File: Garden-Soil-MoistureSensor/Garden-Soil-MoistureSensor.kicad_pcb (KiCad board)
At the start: 2 copper layers, 6 parts, among them J1 Conn_01x15, J2 Conn_01x15, J3 Screw_Terminal_01x02, J4 Screw_Terminal_01x02, Q1 BD140

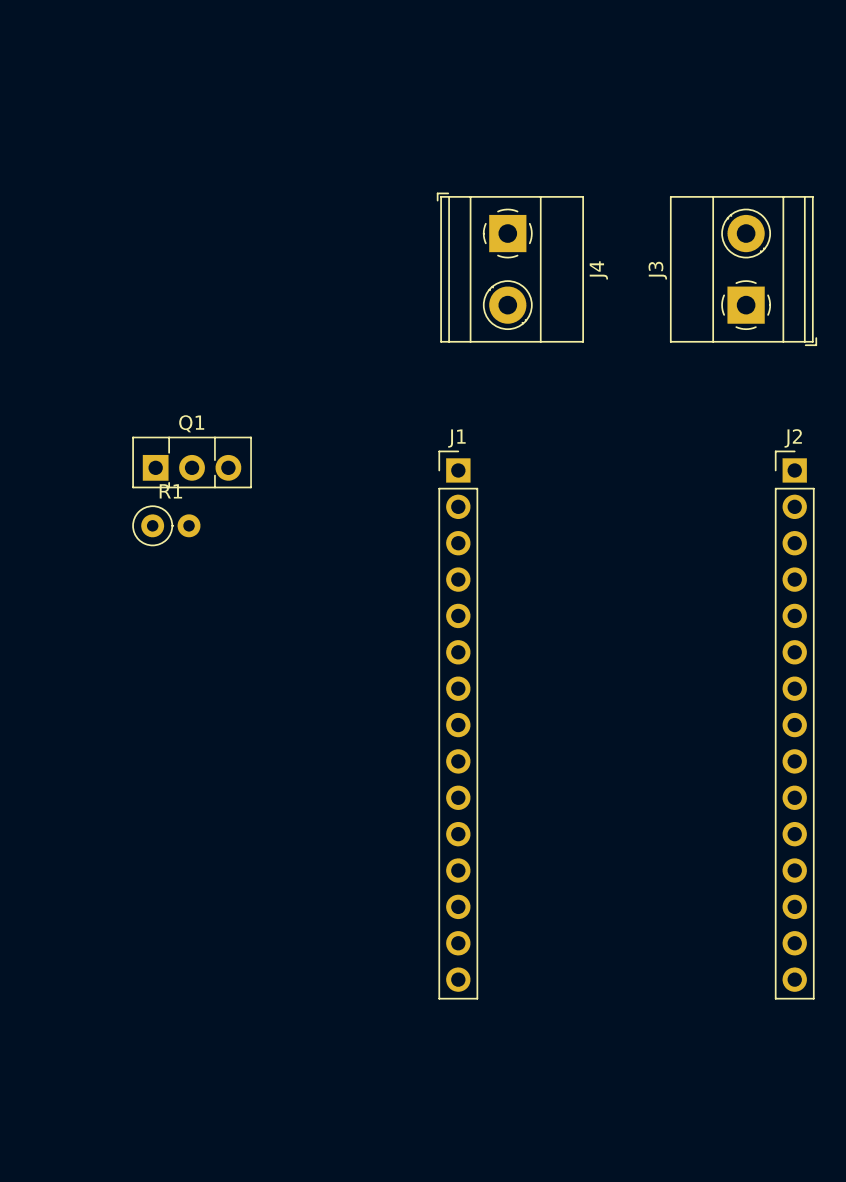
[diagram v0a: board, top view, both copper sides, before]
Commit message: adding a PCB mount 18650 battery holder.
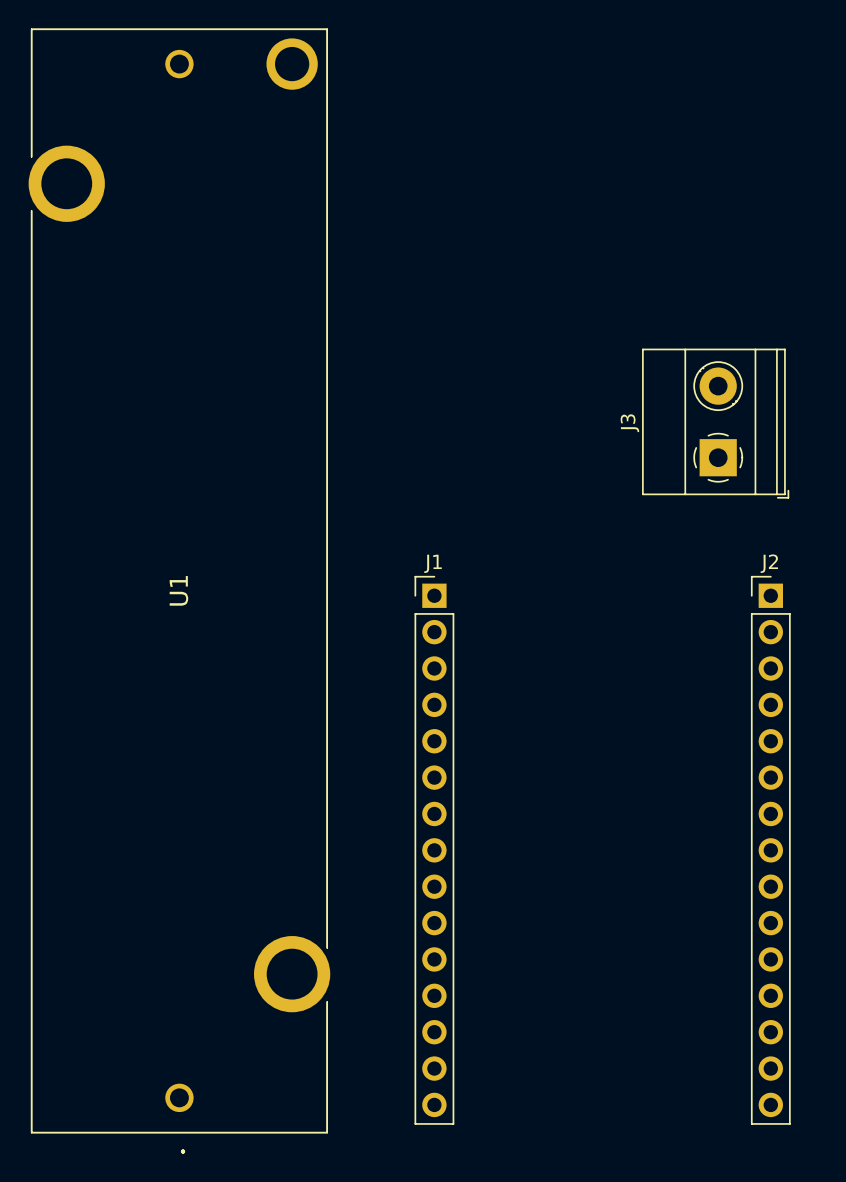
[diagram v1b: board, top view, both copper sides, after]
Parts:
- removed J4: Screw_Terminal_01x02, TerminalBlock_Phoenix:TerminalBlock_Phoenix_MKDS-1,5-2_1x02_P5.00mm_Horizontal
- removed Q1: BD140, Package_TO_SOT_THT:TO-126-3_Vertical
- removed R1: 4.7K, Resistor_THT:R_Axial_DIN0207_L6.3mm_D2.5mm_P2.54mm_Vertical
- added U1: 1043, SamacSys_Parts:1043, F.Cu at (132.9, 130.2)
- moved J3 10.8 mm to (170.6, 85.5)
- moved J1 8.91 mm to (150.7, 95.1)
- moved J2 8.91 mm to (174.2, 95.1)

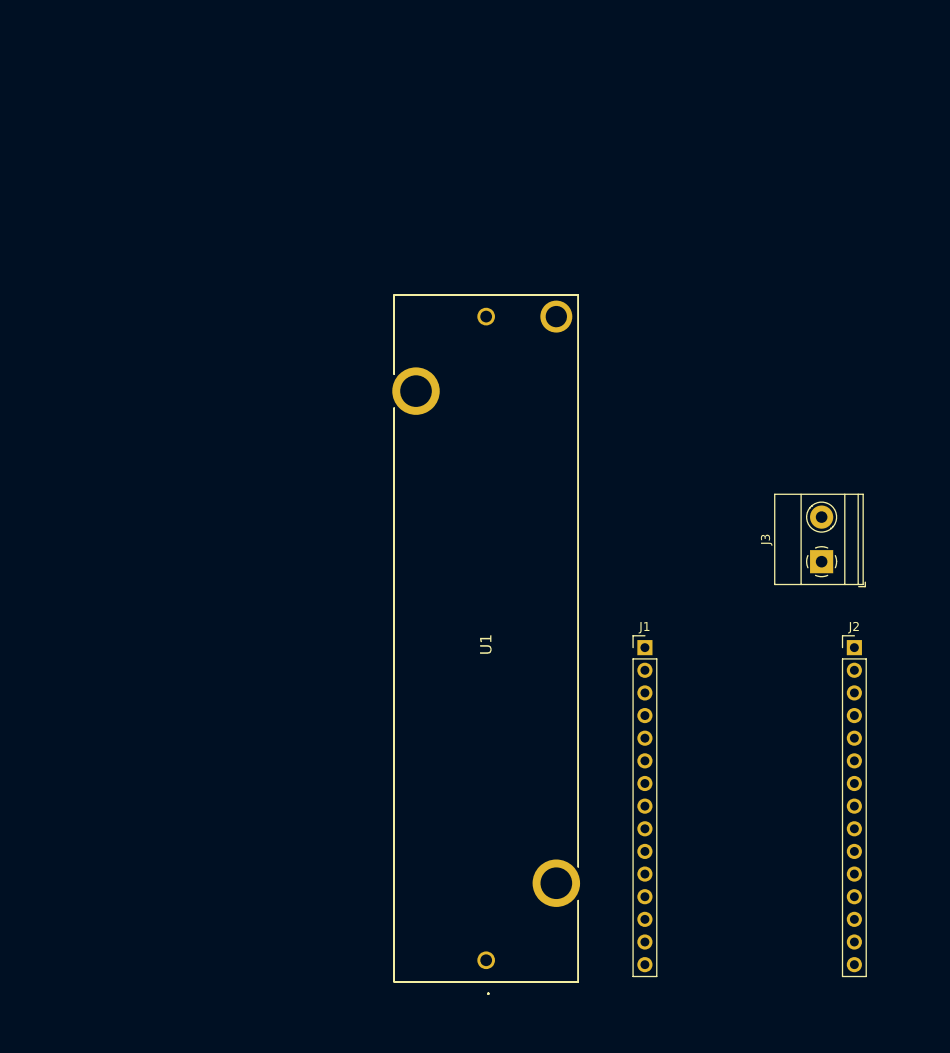
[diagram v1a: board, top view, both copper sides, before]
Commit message: doing some routing and footprint assignments.
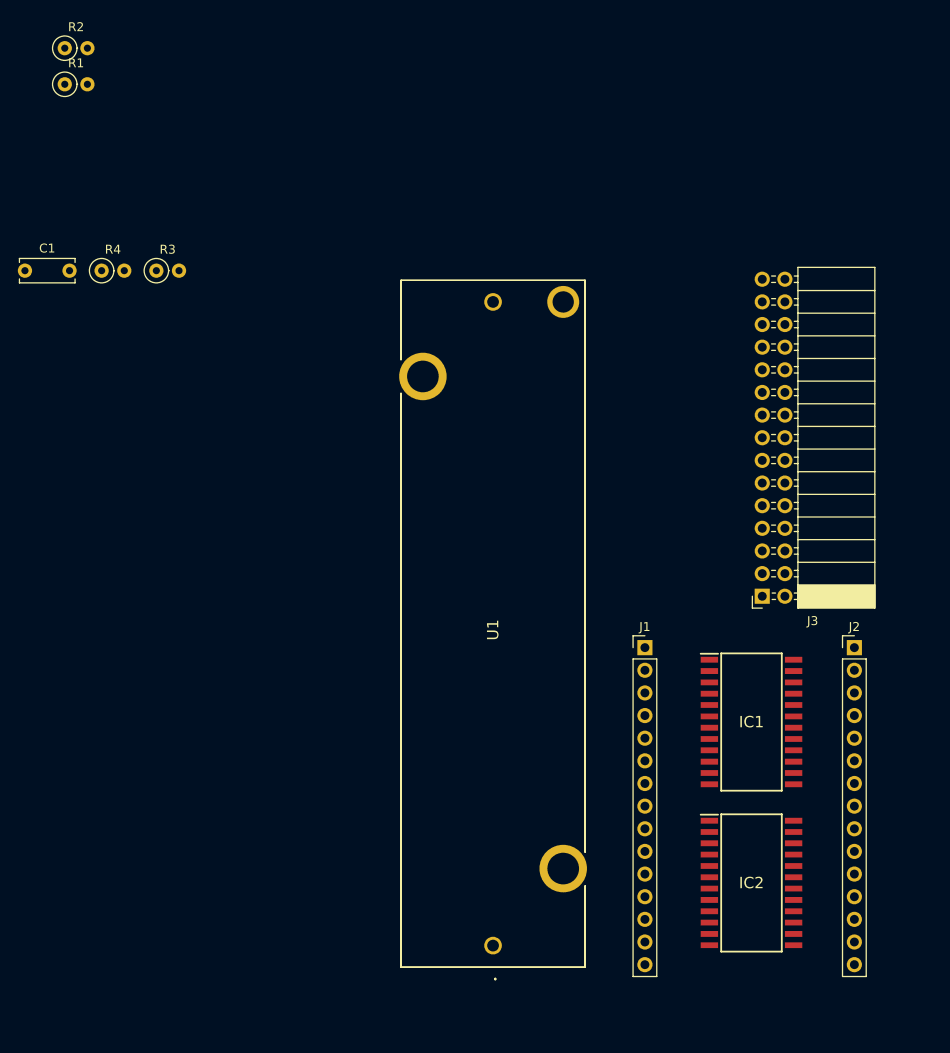
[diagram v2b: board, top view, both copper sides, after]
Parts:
- added C1: 0.1uF, Capacitor_THT:C_Disc_D6.0mm_W2.5mm_P5.00mm, F.Cu at (81.2, 52.8)
- added IC1: CD74HC4067M96, SamacSys_Parts:SOIC127P1030X265-24N, F.Cu at (162.7, 103.5)
- added IC2: CD74HC4067M96, SamacSys_Parts:SOIC127P1030X265-24N, F.Cu at (162.7, 121.5)
- added R1: 1M, Resistor_THT:R_Axial_DIN0207_L6.3mm_D2.5mm_P2.54mm_Vertical, F.Cu at (85.7, 31.9)
- added R2: 10K, Resistor_THT:R_Axial_DIN0207_L6.3mm_D2.5mm_P2.54mm_Vertical, F.Cu at (85.7, 27.9)
- added R3: 10k, Resistor_THT:R_Axial_DIN0207_L6.3mm_D2.5mm_P2.54mm_Vertical, F.Cu at (95.9, 52.8)
- added R4: 10k, Resistor_THT:R_Axial_DIN0207_L6.3mm_D2.5mm_P2.54mm_Vertical, F.Cu at (89.8, 52.8)
- J3: value Screw_Terminal_01x02 -> Conn_02x15_Odd_Even; footprint TerminalBlock_Phoenix:TerminalBlock_Phoenix_MKDS-1,5-2_1x02_P5.00mm_Horizontal -> Connector_PinSocket_2.54mm:PinSocket_2x15_P2.54mm_Horizontal
- moved J3 7.71 mm to (163.9, 89.3), turned to 180 degrees
- moved U1 1.82 mm to (133.7, 128.5)
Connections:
- J3 pad 1: D3 -> 1B
- J3 pad 2: A0 -> 1A
- U1 pad MH1: unconnected-(U1-PadMH1) -> VIN
- U1 pad MH2: unconnected-(U1-PadMH2) -> GND
- U1 pad MH3: unconnected-(U1-PadMH3) -> GND

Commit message: basic placement pre route
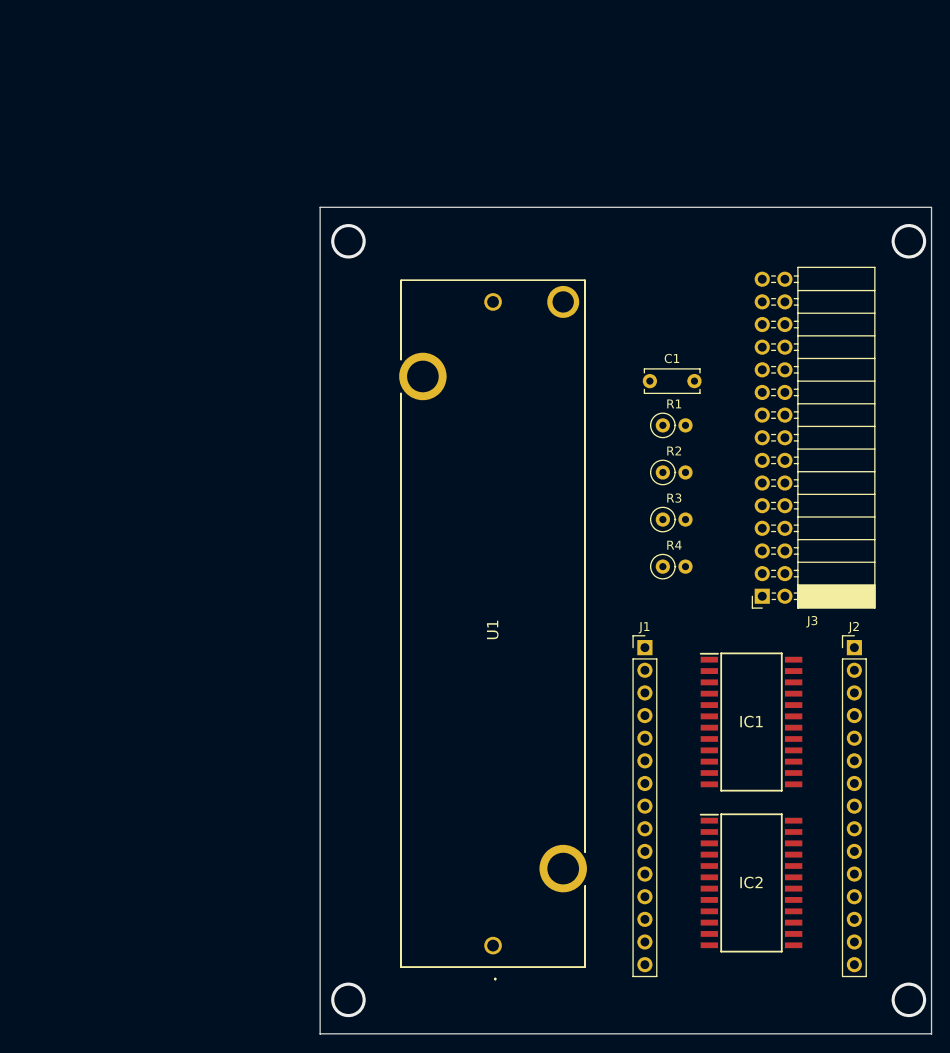
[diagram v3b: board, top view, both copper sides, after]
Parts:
- moved R2 82.3 mm to (152.7, 75.5)
- moved R1 77.2 mm to (152.7, 70.2)
- moved C1 71.2 mm to (151.3, 65.2)
- moved R4 71.2 mm to (152.7, 86.0)
- moved R3 63.3 mm to (152.7, 80.7)
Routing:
- net GND: vias 0 -> 4
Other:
- board outline added: 68.6 x 92.8 mm
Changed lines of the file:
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@@
   (net 33 "2B")
   (net 34 "1B")
-  (net 35 "Net-(IC2-Pad9)")
+  (net 35 "Net-(IC1-Pad9)")
   (net 36 "15B")
   (net 37 "14B")
@@
   (net 58 "8A")
   (footprint "Resistor_THT:R_Axial_DIN0207_L6.3mm_D2.5mm_P2.54mm_Vertical" (layer "F.Cu")
-    (at 89.78908 52.826146)
+    (at 152.742764 86.023614)
     (descr "Resistor, Axial_DIN0207 series, Axial, Vertical, pin pitch=2.54mm, 0.25W = 1/4W, length*diameter=6.3*2.5mm^2, http://cdn-reichelt.de/documents/datenblatt/B400/1_4W%23YAG.pdf")
     (tags "Resistor Axial_DIN0207 series Axial Vertical pin pitch 2.54mm 0.25W = 1/4W length 6.3mm diameter 2.5mm")
@@
   )
   (footprint "Resistor_THT:R_Axial_DIN0207_L6.3mm_D2.5mm_P2.54mm_Vertical" (layer "F.Cu")
-    (at 85.654047 27.869494)
+    (at 152.742764 75.462029)
     (descr "Resistor, Axial_DIN0207 series, Axial, Vertical, pin pitch=2.54mm, 0.25W = 1/4W, length*diameter=6.3*2.5mm^2, http://cdn-reichelt.de/documents/datenblatt/B400/1_4W%23YAG.pdf")
     (tags "Resistor Axial_DIN0207 series Axial Vertical pin pitch 2.54mm 0.25W = 1/4W length 6.3mm diameter 2.5mm")
@@
   )
   (footprint "Resistor_THT:R_Axial_DIN0207_L6.3mm_D2.5mm_P2.54mm_Vertical" (layer "F.Cu")
-    (at 85.654047 31.919494)
+    (at 152.742764 70.181237)
     (descr "Resistor, Axial_DIN0207 series, Axial, Vertical, pin pitch=2.54mm, 0.25W = 1/4W, length*diameter=6.3*2.5mm^2, http://cdn-reichelt.de/documents/datenblatt/B400/1_4W%23YAG.pdf")
     (tags "Resistor Axial_DIN0207 series Axial Vertical pin pitch 2.54mm 0.25W = 1/4W length 6.3mm diameter 2.5mm")
@@
   )
   (footprint "Resistor_THT:R_Axial_DIN0207_L6.3mm_D2.5mm_P2.54mm_Vertical" (layer "F.Cu")
-    (at 95.92908 52.826146)
+    (at 152.742764 80.742821)
     (descr "Resistor, Axial_DIN0207 series, Axial, Vertical, pin pitch=2.54mm, 0.25W = 1/4W, length*diameter=6.3*2.5mm^2, http://cdn-reichelt.de/documents/datenblatt/B400/1_4W%23YAG.pdf")
     (tags "Resistor Axial_DIN0207 series Axial Vertical pin pitch 2.54mm 0.25W = 1/4W length 6.3mm diameter 2.5mm")
@@
       (net 34 "1B") (pinfunction "I1") (pintype "passive"))
     (pad "9" smd rect locked (at -4.725 3.175 90) (size 0.65 1.95) (layers "F.Cu" "F.Paste" "F.Mask")
-      (net 35 "Net-(IC2-Pad9)") (pinfunction "I0") (pintype "passive"))
+      (net 35 "Net-(IC1-Pad9)") (pinfunction "I0") (pintype "passive"))
     (pad "10" smd rect locked (at -4.725 4.445 90) (size 0.65 1.95) (layers "F.Cu" "F.Paste" "F.Mask")
       (net 15 "D1") (pinfunction "S0") (pintype "passive"))
@@
   )
   (footprint "Capacitor_THT:C_Disc_D6.0mm_W2.5mm_P5.00mm" (layer "F.Cu")
-    (at 81.18908 52.826146)
+    (at 151.287764 65.215488)
     (descr "C, Disc series, Radial, pin pitch=5.00mm, , diameter*width=6*2.5mm^2, Capacitor, http://cdn-reichelt.de/documents/datenblatt/B300/DS_KERKO_TC.pdf")
     (tags "C Disc series Radial pin pitch 5.00mm  diameter 6mm width 2.5mm Capacitor")
@@
       (net 50 "1A") (pinfunction "I1") (pintype "passive"))
     (pad "9" smd rect locked (at -4.725 3.175 90) (size 0.65 1.95) (layers "F.Cu" "F.Paste" "F.Mask")
-      (net 35 "Net-(IC2-Pad9)") (pinfunction "I0") (pintype "passive"))
+      (net 35 "Net-(IC1-Pad9)") (pinfunction "I0") (pintype "passive"))
     (pad "10" smd rect locked (at -4.725 4.445 90) (size 0.65 1.95) (layers "F.Cu" "F.Paste" "F.Mask")
       (net 15 "D1") (pinfunction "S0") (pintype "passive"))
@@
     )
   )
+  (gr_line (start 114.3 45.72) (end 114.3 138.475913) (layer "Edge.Cuts") (width 0.1))
+  (gr_line (start 182.88 45.72) (end 114.3 45.72) (layer "Edge.Cuts") (width 0.1))
+  (gr_line (start 114.3 138.43) (end 182.88 138.43) (layer "Edge.Cuts") (width 0.1))
+  (gr_line (start 182.88 138.48139) (end 182.88 45.754492) (layer "Edge.Cuts") (width 0.1))
+  (via (at 117.475 49.53) (size 3.8736) (drill 3.175) (layers "F.Cu" "B.Cu") (free) (net 10))
+  (via (at 117.475 134.62) (size 3.8736) (drill 3.175) (layers "F.Cu" "B.Cu") (free) (net 10))
+  (via (at 180.34 49.53) (size 3.8736) (drill 3.175) (layers "F.Cu" "B.Cu") (free) (net 10))
+  (via (at 180.34 134.62) (size 3.8736) (drill 3.175) (layers "F.Cu" "B.Cu") (free) (net 10))
   (group "" (id 31916c38-883f-4186-ab10-8bd6d91959f5)
     (members

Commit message: drc fixes pre route
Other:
- board size 68.6 x 92.8 mm -> 68.6 x 92.7 mm
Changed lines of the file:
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@@
     )
   )
-  (gr_line (start 114.3 45.72) (end 114.3 138.475913) (layer "Edge.Cuts") (width 0.1))
+  (gr_line (start 114.3 45.72) (end 114.3 138.43) (layer "Edge.Cuts") (width 0.1))
   (gr_line (start 182.88 45.72) (end 114.3 45.72) (layer "Edge.Cuts") (width 0.1))
   (gr_line (start 114.3 138.43) (end 182.88 138.43) (layer "Edge.Cuts") (width 0.1))
-  (gr_line (start 182.88 138.48139) (end 182.88 45.754492) (layer "Edge.Cuts") (width 0.1))
+  (gr_line (start 182.88 138.43) (end 182.88 45.72) (layer "Edge.Cuts") (width 0.1))
   (via (at 117.475 49.53) (size 3.8736) (drill 3.175) (layers "F.Cu" "B.Cu") (free) (net 10))
   (via (at 117.475 134.62) (size 3.8736) (drill 3.175) (layers "F.Cu" "B.Cu") (free) (net 10))

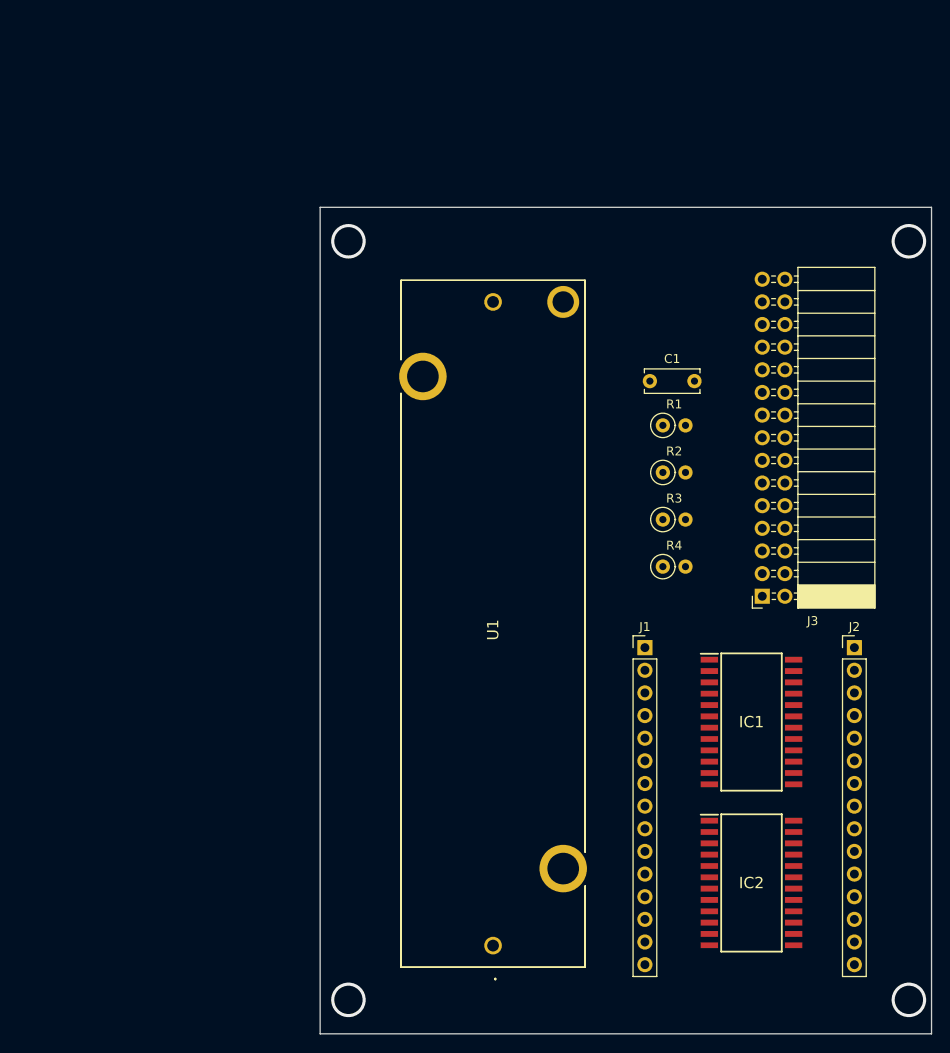
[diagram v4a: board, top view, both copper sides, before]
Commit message: post route needs to have silkscreen labels applied.
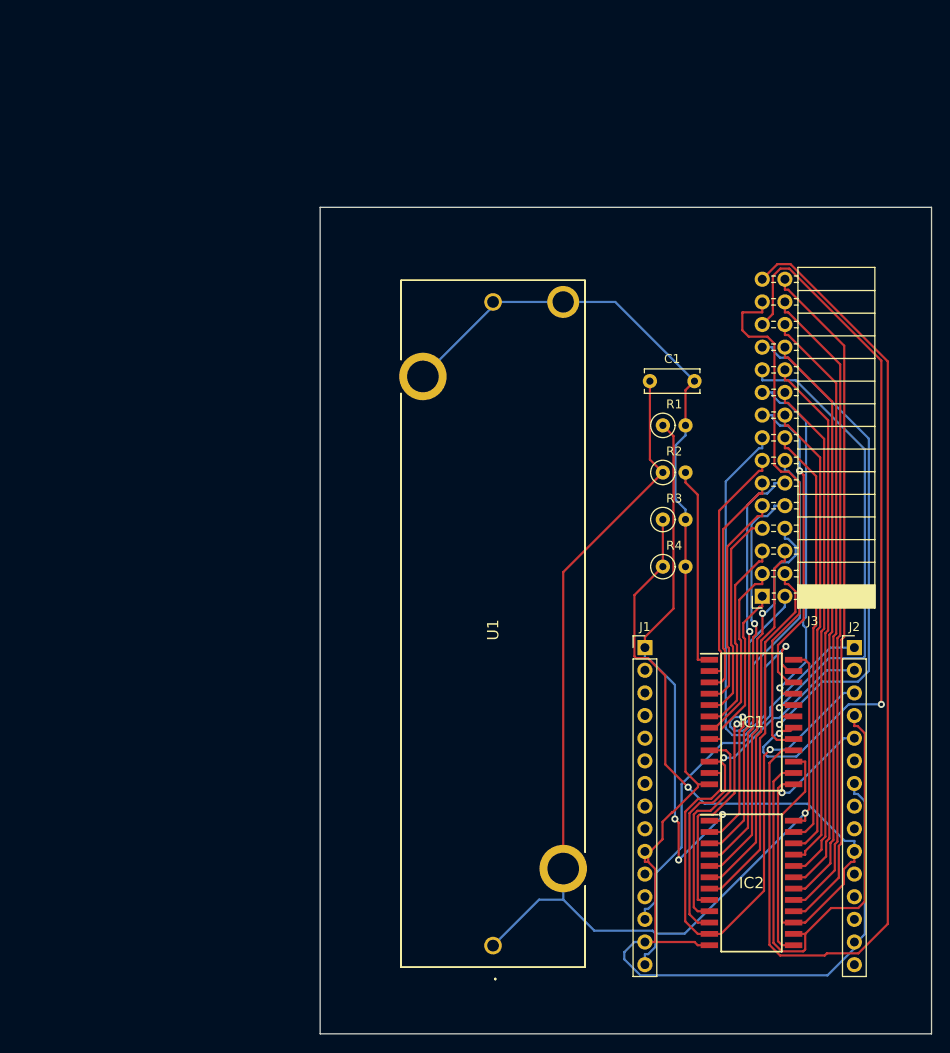
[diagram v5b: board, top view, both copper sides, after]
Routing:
- net GND: track 0.00 -> 165.9 mm, vias 4 -> 0
- net VIN: track 0.00 -> 132.9 mm, vias 0 -> 1
- net 15B: track 0.00 -> 121.3 mm
- net D7: track 0.00 -> 89.8 mm, vias 0 -> 1
- net 13B: track 0.00 -> 82.0 mm, vias 0 -> 2
- net 15A: track 0.00 -> 77.0 mm
- net 14A: track 0.00 -> 72.8 mm
- net 13A: track 0.00 -> 68.6 mm
- net 12A: track 0.00 -> 64.4 mm
- net A0: track 0.00 -> 61.6 mm, vias 0 -> 3
- net 11A: track 0.00 -> 60.2 mm
- net D2: track 0.00 -> 59.4 mm, vias 0 -> 1
- net 14B: track 0.00 -> 59.0 mm
- net D3: track 0.00 -> 57.6 mm
- net 12B: track 0.00 -> 57.3 mm, vias 0 -> 1
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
